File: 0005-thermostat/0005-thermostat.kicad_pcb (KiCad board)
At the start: 2 copper layers, 70 x 60 mm, 45 parts, among them J1 EXT_NTC, J2 OUT, J3 PWR, J4 EXT_LED, J5 EXT_P1, J6 EXT_P2, P1 22k, P2 22k, T1 BC847B, T2 BC847B, T3 BC847B

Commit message: Redesign another sections
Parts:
- moved J5 101.3 mm to (120.7, 131.9)
- moved P1 82.4 mm to (116.3, 122.5), turned to 180 degrees
- moved J6 80.3 mm to (131.5, 131.8)
- moved JP2 70.2 mm to (122.0, 121.3), turned to 180 degrees
- moved P2 69.8 mm to (127.9, 122.5), turned to 180 degrees
- moved J1 68.2 mm to (141.9, 131.8)
- moved R3 58.1 mm to (137.0, 114.4), turned to -90 degrees
- moved NTC1 52.7 mm to (139.8, 124.4)
- moved C1 52.4 mm to (146.0, 119.4)
- moved R2 50.9 mm to (131.6, 114.4), turned to -90 degrees
- moved JP1 48.9 mm to (146.9, 125.0), turned to 90 degrees
- moved R1 47.4 mm to (139.8, 118.8), turned to 180 degrees
- moved R4 6.19 mm to (123.6, 86.3)
- moved REF** 5.38 mm to (104.0, 131.4)
- moved REF** 4.00 mm to (104.0, 85.0)
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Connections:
- J1 pad MP: (no net) -> GNDD
- J5 pad MP: (no net) -> GNDD
- J6 pad MP: (no net) -> GNDD
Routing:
- net Net-(J1-Pin_1): track 0.00 -> 126.0 mm
- net Net-(J6-Pin_1): track 0.00 -> 116.4 mm, vias 0 -> 2
- net Net-(J5-Pin_1): track 0.00 -> 110.8 mm
- net Net-(C5-Pad1): track 32.8 -> 85.2 mm, vias 2 -> 3
- net +12V: track 161.1 -> 188.6 mm
- net Net-(JP2-B): track 0.00 -> 19.7 mm
- net Net-(C4-Pad1): track 41.8 -> 48.3 mm
- net Net-(JP1-B): track 0.00 -> 6.19 mm
- net Net-(D1-A): track 87.4 -> 83.8 mm
- net Net-(D2-A): track 100.4 -> 96.8 mm
- net Net-(D3-A): track 119.3 -> 115.8 mm
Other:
- board size 70 x 60 mm -> 70 x 69.9 mm

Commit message: Re-design comparator section, shrink the board
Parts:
- added ?: , , F.Cu at (107.8, 125.7)
- added ?: , , F.Cu at (162.1, 90.7)
- added ?: , , F.Cu at (143.0, 102.5)
- added ?: , , F.Cu at (162.1, 126.0)
- added ?: , , F.Cu at (134.3, 108.5)
- added ?: , , F.Cu at (114.7, 83.4)
- moved C1 89.8 mm to (67.0, 76.7)
- moved NTC1 83.2 mm to (67.0, 84.2)
- moved J1 83.0 mm to (68.2, 93.6)
- moved R1 79.6 mm to (67.0, 86.7), turned to 0 degrees
- moved R3 75.7 mm to (71.3, 76.7), turned to 0 degrees
- moved JP1 71.9 mm to (84.3, 89.7), turned to 0 degrees
- moved J6 71.7 mm to (77.4, 84.8)
- moved R2 69.4 mm to (67.0, 89.2), turned to 0 degrees
- moved J5 68.7 mm to (77.4, 78.5)
- moved P2 57.7 mm to (84.5, 84.5), turned to 0 degrees
- moved P1 54.4 mm to (84.5, 78.4), turned to 0 degrees
- moved JP2 47.0 mm to (84.3, 93.2), turned to 0 degrees
- moved R7 16.3 mm to (129.9, 85.1)
- moved R5 8.58 mm to (112.3, 98.0)
- moved US1 5.35 mm to (120.8, 92.7)
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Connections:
- J1 pad MP: GNDD -> (no net)
- J5 pad MP: GNDD -> (no net)
- J6 pad MP: GNDD -> (no net)
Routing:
- net Net-(J5-Pin_1): track 110.8 -> 31.2 mm
- net Net-(J1-Pin_1): track 126.0 -> 48.3 mm
- net Net-(J6-Pin_1): track 116.4 -> 39.2 mm, vias 2 -> 1
- net Net-(JP2-B): track 19.7 -> 0.00 mm
- net Net-(C5-Pad1): track 85.2 -> 76.2 mm
- net Net-(R9-Pad1): track 34.1 -> 41.6 mm
- net Net-(JP1-B): track 6.19 -> 0.00 mm
- net Net-(D1-A): track 83.8 -> 81.3 mm
- net Net-(D2-A): track 96.8 -> 98.8 mm
- net +12V: track 188.6 -> 186.8 mm
- net GNDD: track 12.8 -> 11.7 mm
- added copper zone on B.Cu, net GNDD
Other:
- board size 70 x 69.9 mm -> 61 x 56 mm

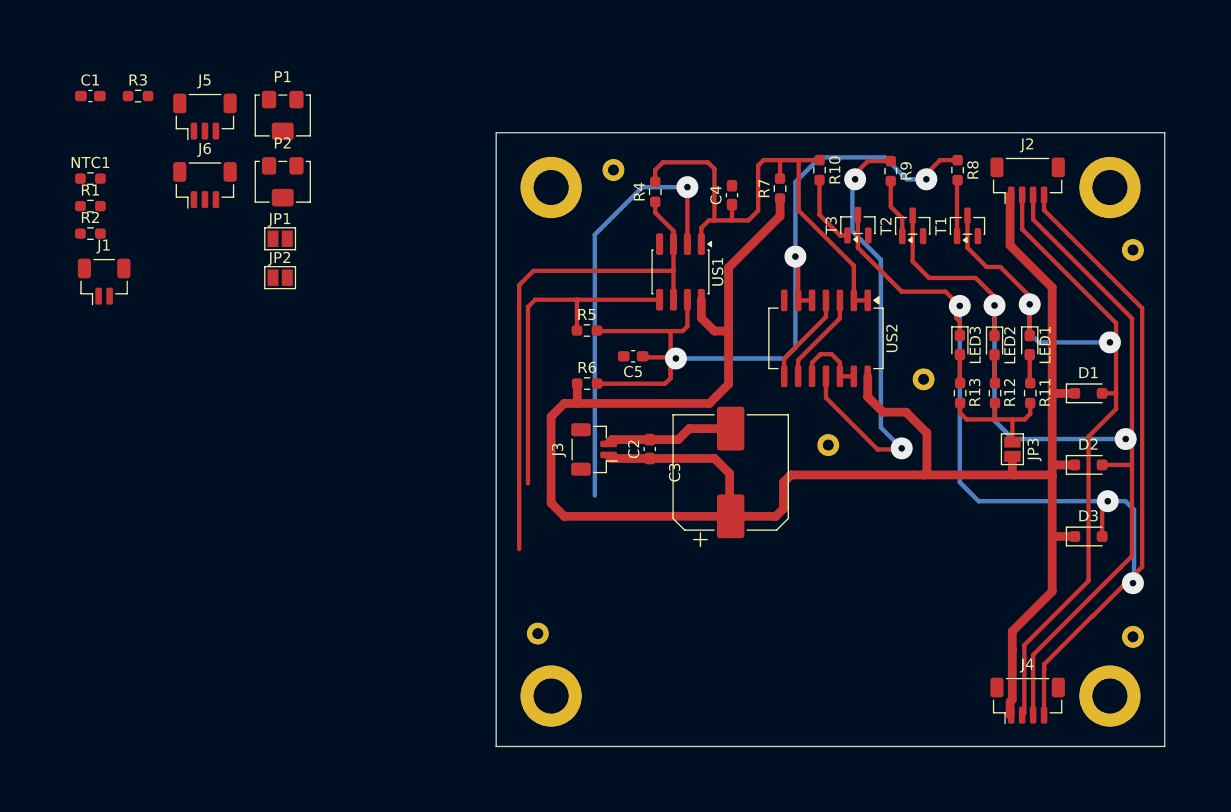
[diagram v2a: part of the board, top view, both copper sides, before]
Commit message: Redesigned PCB shape
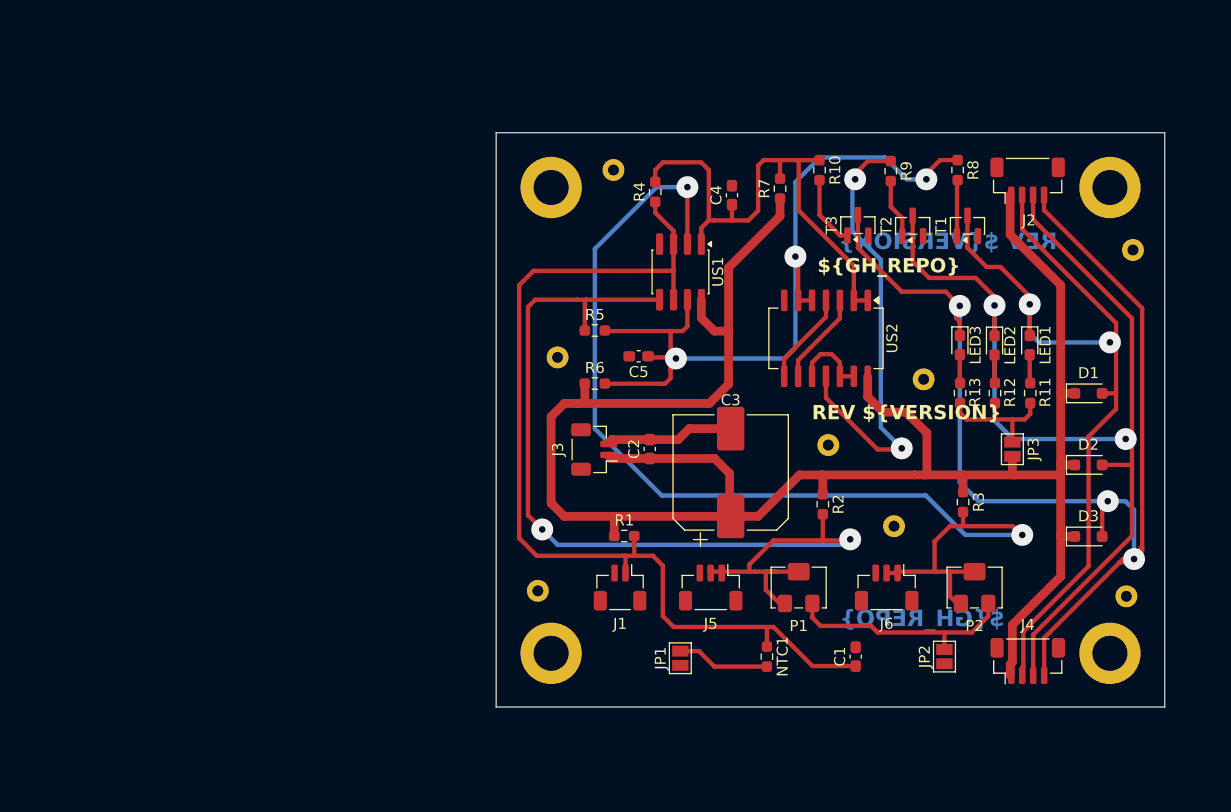
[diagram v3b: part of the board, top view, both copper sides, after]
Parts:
- added ?: , , F.Cu at (109.6, 100.5)
- added ?: , , F.Cu at (140.3, 115.9)
- moved C1 86.6 mm to (136.8, 127.8), turned to 90 degrees
- moved R3 83.9 mm to (146.6, 113.7), turned to -90 degrees
- moved NTC1 75.6 mm to (128.7, 127.8), turned to -90 degrees
- moved P2 73.2 mm to (147.7, 121.5), turned to 180 degrees
- moved J6 72.2 mm to (139.6, 121.5), turned to 180 degrees
- moved R2 71.2 mm to (133.8, 113.9), turned to -90 degrees
- moved JP2 69.8 mm to (144.9, 127.8), turned to 90 degrees
- moved P1 63.8 mm to (131.6, 121.5), turned to 180 degrees
- moved J5 63.1 mm to (123.6, 121.5), turned to 180 degrees
- moved R1 57.3 mm to (115.7, 116.8)
- moved J1 54.7 mm to (115.3, 121.5), turned to 180 degrees
- moved JP1 52.9 mm to (120.8, 128.0), turned to 90 degrees
- moved ? 3.90 mm to (107.8, 121.8)
- moved REF** 3.90 mm to (109.0, 127.5)
- moved REF** 3.90 mm to (160.0, 127.5)
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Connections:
- J1 pad MP: (no net) -> GNDD
- J5 pad MP: (no net) -> GNDD
- J6 pad MP: (no net) -> GNDD
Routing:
- net Net-(J6-Pin_1): track 39.2 -> 100.6 mm, vias 1 -> 2
- net Net-(J5-Pin_1): track 31.2 -> 91.6 mm, vias 0 -> 2
- net Net-(J1-Pin_1): track 48.3 -> 90.8 mm
- net Net-(JP2-B): track 0.00 -> 21.2 mm
- net Net-(JP1-B): track 0.00 -> 8.49 mm
- net Net-(D2-A): track 98.8 -> 95.2 mm
- net Net-(D1-A): track 81.3 -> 77.6 mm
- net Net-(D3-A): track 115.9 -> 113.7 mm
- net Net-(C5-Pad1): track 76.2 -> 74.7 mm
- net +12V: track 186.8 -> 186.2 mm
- net Net-(C4-Pad1): track 48.3 -> 47.7 mm
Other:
- board size 61 x 56 mm -> 61 x 52.4 mm
- board text added: "${GH_REPO}"
- board text added: "REV ${VERSION}"

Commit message: Replace SOIC to TSSOP ICs footprints
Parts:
- US1: footprint Package_SO:SOP-8_3.76x4.96mm_P1.27mm -> Package_SO:TSSOP-8_4.4x3mm_P0.65mm
- US2: footprint Package_SO:SO-14_5.3x10.2mm_P1.27mm -> Package_SO:TSSOP-14_4.4x5mm_P0.65mm
- moved NTC1 24.5 mm to (152.4, 121.7)
- moved R11 24.5 mm to (176.5, 97.6)
- moved R12 24.5 mm to (173.2, 97.6)
- moved ? 24.5 mm to (131.5, 115.7)
- moved ? 24.5 mm to (138.4, 77.3)
- moved C2 24.5 mm to (141.7, 102.7)
- moved C3 24.5 mm to (149.1, 104.9)
- moved C4 24.5 mm to (149.2, 79.6)
- moved J1 24.5 mm to (139.0, 115.4)
- moved J5 24.5 mm to (147.3, 115.4)
- moved JP1 24.5 mm to (144.5, 121.8)
- moved R4 24.5 mm to (142.2, 79.3)
- moved REF** 24.5 mm to (132.7, 121.4)
- moved REF** 24.5 mm to (132.7, 78.9)
- moved ? 24.5 mm to (185.8, 84.6)
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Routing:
- net +12V: track 186.2 -> 190.8 mm
- net Net-(US2-Pad10): track 6.96 -> 4.93 mm
- net Net-(US2-Pad4): track 8.50 -> 6.53 mm
- net Net-(US2-Pad3): track 8.50 -> 6.53 mm
- net Net-(J1-Pin_1): track 90.8 -> 92.3 mm
- net Net-(J5-Pin_1): track 91.6 -> 92.7 mm
- net Net-(C5-Pad1): track 74.7 -> 74.2 mm
